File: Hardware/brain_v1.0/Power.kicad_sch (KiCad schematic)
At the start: 47 parts, among them J1 Conn_01x02, J10 Barrel_Jack, U1 MP2338GTL-Z, U2 MP2315SGJ-Z, U3 AMS1117-3.3

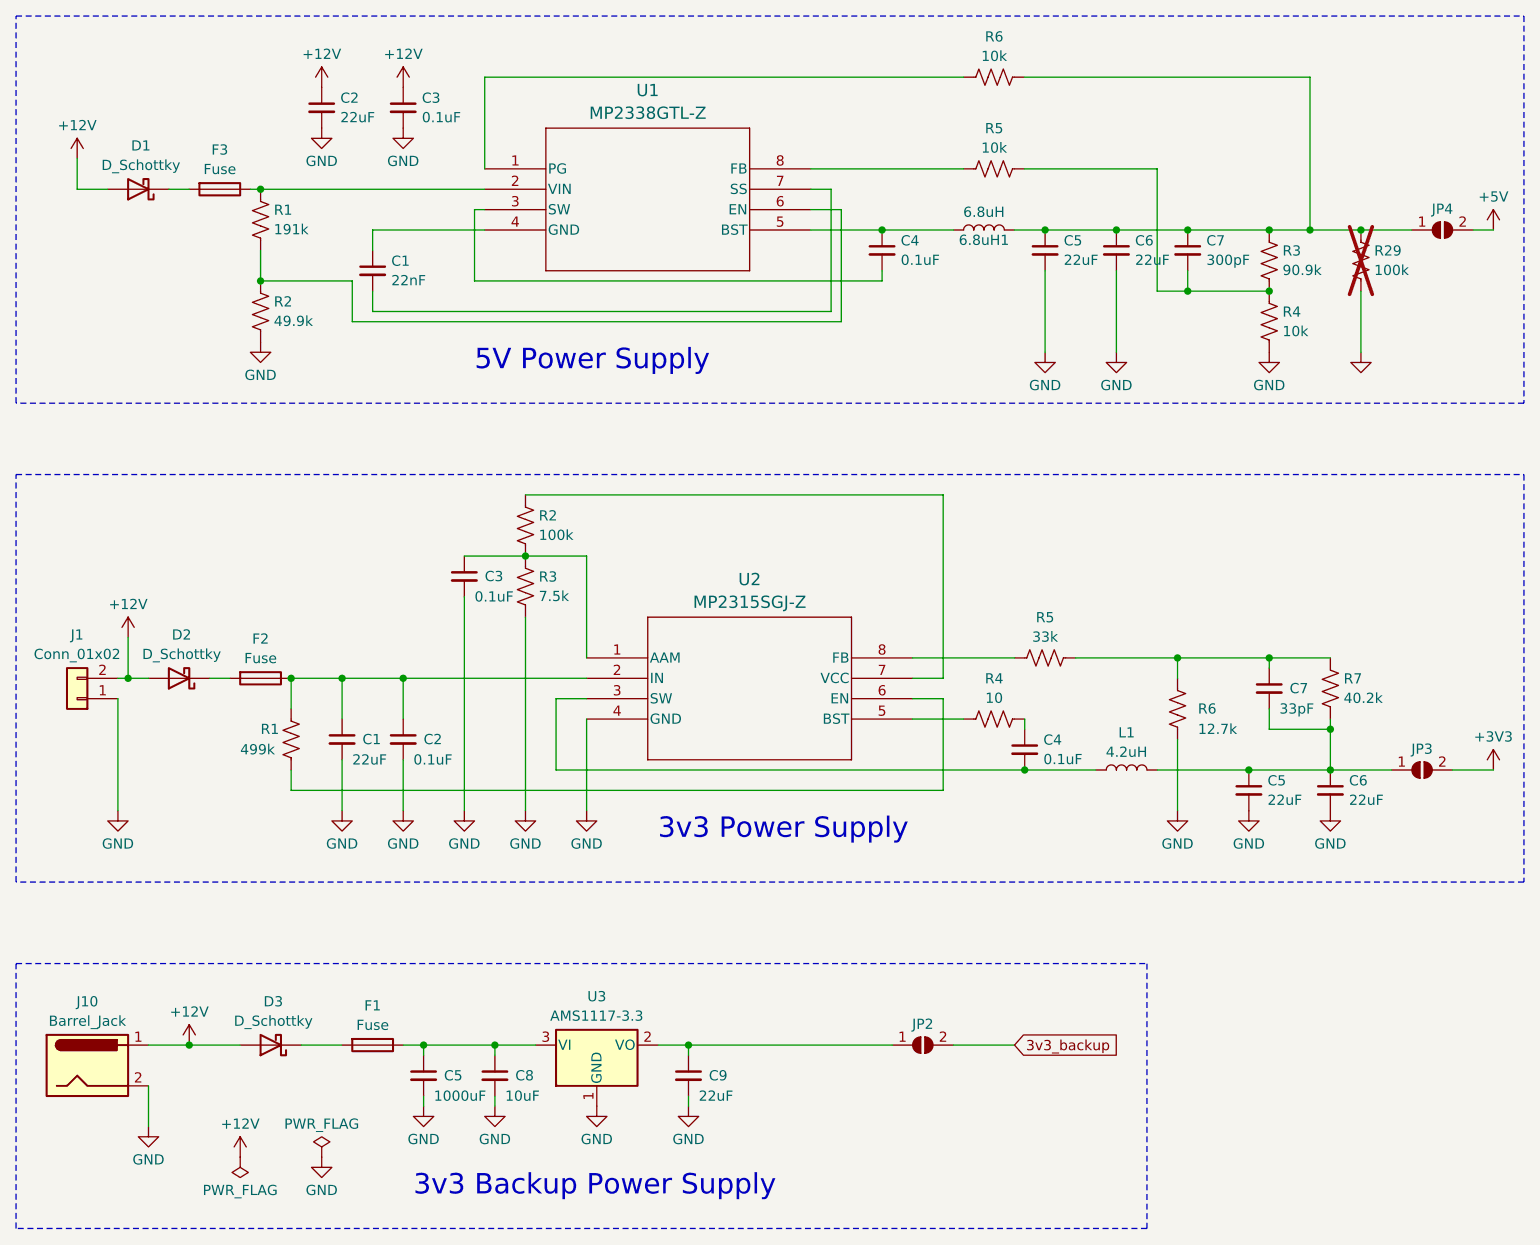
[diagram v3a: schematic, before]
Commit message: finished part selection and schematic for brain. Created RFID and Motor Driver boards
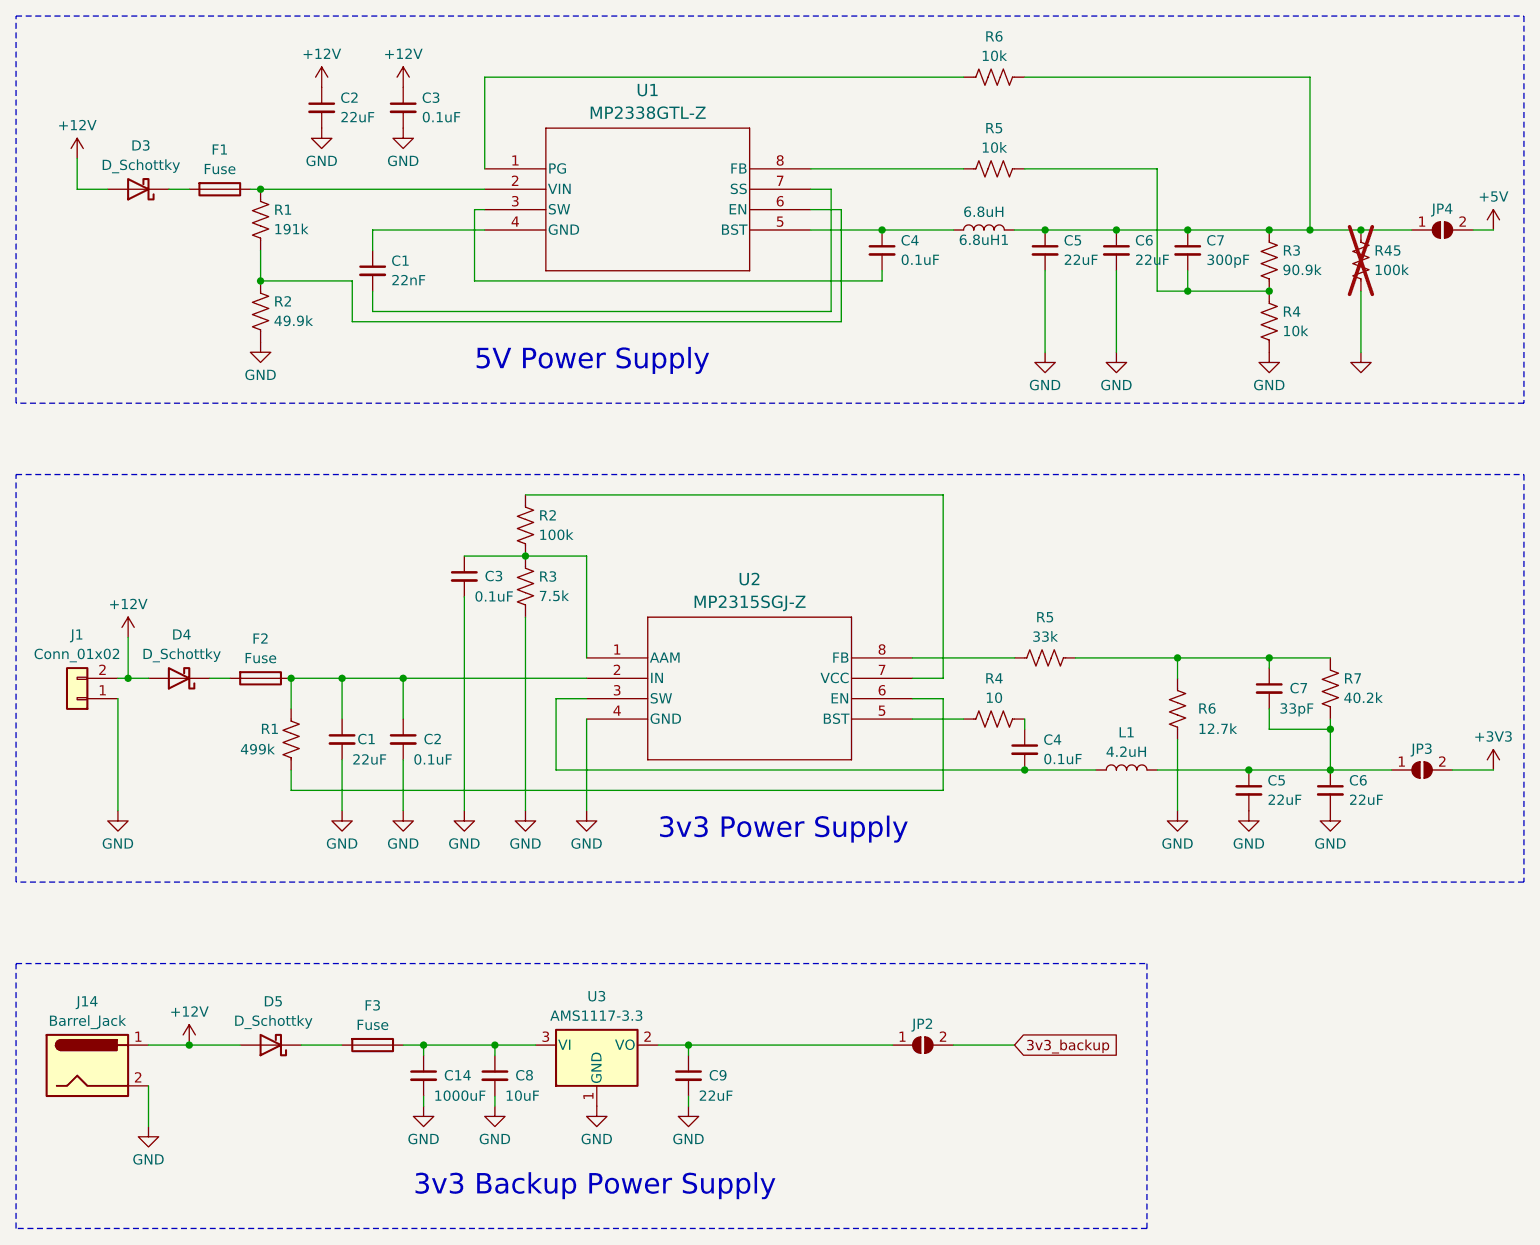
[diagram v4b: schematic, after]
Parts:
- renumbered C5 to C14, D1 to D3, D2 to D4, D3 to D5, F3 to F1, F1 to F3, J10 to J14, R29 to R45

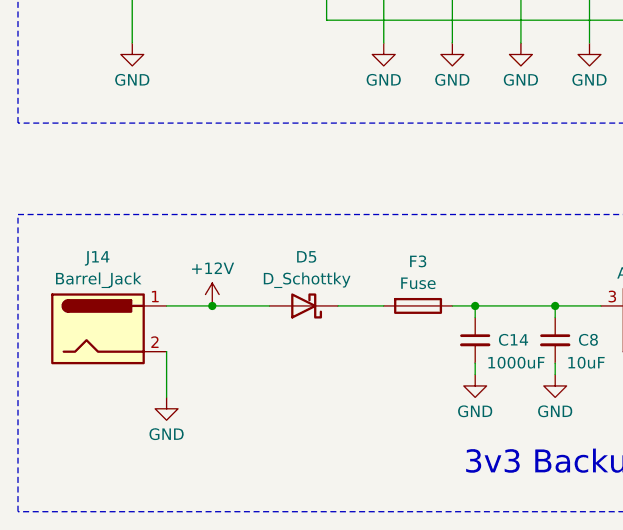
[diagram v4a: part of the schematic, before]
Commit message: brain fix and almost done with power board layout
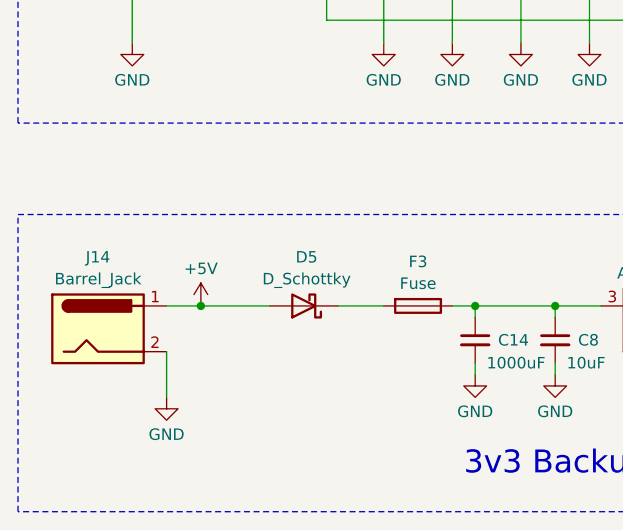
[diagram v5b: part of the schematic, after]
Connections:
- net +12V: no longer D5.2 (A), J14.1
- net +5V: now also D5.2 (A), J14.1
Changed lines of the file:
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@@
   (junction (at 81.28 86.36) (diameter 0) (color 0 0 0 0)
   )
-  (junction (at 39.37 147.32) (diameter 0) (color 0 0 0 0)
-  )
   (junction (at 66.04 101.6) (diameter 0) (color 0 0 0 0)
   )
@@
   (junction (at 146.05 45.72) (diameter 0) (color 0 0 0 0)
   )
+  (junction (at 38.1 147.32) (diameter 0) (color 0 0 0 0)
+  )
   (junction (at 171.45 113.03) (diameter 0) (color 0 0 0 0)
   )
@@
     (stroke (width 0) (type default))
   )
-  (wire (pts (xy 34.29 147.32) (xy 39.37 147.32))
-    (stroke (width 0) (type default))
-  )
   (wire (pts (xy 179.07 26.67) (xy 179.07 45.72))
     (stroke (width 0) (type default))
@@
     (stroke (width 0) (type default))
   )
+  (wire (pts (xy 38.1 147.32) (xy 45.72 147.32))
+    (stroke (width 0) (type default))
+  )
   (wire (pts (xy 66.04 111.76) (xy 66.04 118.11))
     (stroke (width 0) (type default))
@@
     (stroke (width 0) (type default))
   )
-  (wire (pts (xy 39.37 147.32) (xy 45.72 147.32))
+  (wire (pts (xy 34.29 147.32) (xy 38.1 147.32))
     (stroke (width 0) (type default))
   )
@@
         (path "/1e1b062d-fad0-427c-a622-c5b8a80b5268/88dc6c48-fc37-4022-af3c-4da37eedeb92"
           (reference "#PWR071") (unit 1)
+        )
+      )
+    )
+  )
+  (symbol (lib_id "power:+5V") (at 38.1 147.32 0) (unit 1)
+    (in_bom yes) (on_board yes) (dnp no) (fields_autoplaced)
+    (property "Reference" "#PWR058" (at 38.1 151.13 0)
+      (effects (font (size 1.27 1.27)) hide)
+    )
+    (property "Value" "+5V" (at 38.1 143.1869 0)
+      (effects (font (size 1.27 1.27)))
+    )
+    (property "Footprint" "" (at 38.1 147.32 0)
+      (effects (font (size 1.27 1.27)) hide)
+    )
+    (property "Datasheet" "" (at 38.1 147.32 0)
+      (effects (font (size 1.27 1.27)) hide)
+    )
+    (pin "1")
+    (instances
+      (project "brain_v1.0"
+        (path "/1e1b062d-fad0-427c-a622-c5b8a80b5268/88dc6c48-fc37-4022-af3c-4da37eedeb92"
+          (reference "#PWR058") (unit 1)
         )
       )
@@
         )
       )
-    )
-  )
-  (symbol (lib_id "power:+12V") (at 39.37 147.32 0) (unit 1)
-    (in_bom yes) (on_board yes) (dnp no)
-    (property "Reference" "#PWR058" (at 39.37 151.13 0)
-      (effects (font (size 1.27 1.27)) hide)
-    )
-    (property "Value" "+12V" (at 39.37 143.1869 0)
-      (effects (font (size 1.27 1.27)))
-    )
-    (property "Footprint" "" (at 39.37 147.32 0)
-      (effects (font (size 1.27 1.27)) hide)
-    )
-    (property "Datasheet" "" (at 39.37 147.32 0)
-      (effects (font (size 1.27 1.27)) hide)
-    )
-    (pin "1")
-    (instances
-      (project "brain_v1.0"
-        (path "/1e1b062d-fad0-427c-a622-c5b8a80b5268/88dc6c48-fc37-4022-af3c-4da37eedeb92"
-          (reference "#PWR058") (unit 1)
-        )
-      )
